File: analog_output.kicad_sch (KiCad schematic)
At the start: 18 parts, among them J3 5 Pin 3.5mm, U6 LM358, U7 74HC14

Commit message: routed version
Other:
- moved on the sheet: U7D
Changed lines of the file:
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@@
   )
   (no_connect (at 172.72 95.25))
-  (no_connect (at 171.45 110.49))
+  (no_connect (at 173.99 110.49))
   (wire (pts (xy 212.09 107.95) (xy 212.09 118.11))
     (stroke (width 0) (type default))
@@
     )
   )
-  (symbol (lib_id "power:GND") (at 156.21 110.49 270) (mirror x) (unit 1)
-    (in_bom yes) (on_board yes) (dnp no) (fields_autoplaced)
-    (property "Reference" "#PWR0143" (at 149.86 110.49 0)
-      (effects (font (size 1.27 1.27)) hide)
-    )
-    (property "Value" "GND" (at 152.4 110.4899 90)
+  (symbol (lib_id "power:GND") (at 158.75 110.49 270) (mirror x) (unit 1)
+    (in_bom yes) (on_board yes) (dnp no) (fields_autoplaced)
+    (property "Reference" "#PWR0143" (at 152.4 110.49 0)
+      (effects (font (size 1.27 1.27)) hide)
+    )
+    (property "Value" "GND" (at 154.94 110.4899 90)
       (effects (font (size 1.27 1.27)) (justify right))
     )
-    (property "Footprint" "" (at 156.21 110.49 0)
-      (effects (font (size 1.27 1.27)) hide)
-    )
-    (property "Datasheet" "" (at 156.21 110.49 0)
+    (property "Footprint" "" (at 158.75 110.49 0)
+      (effects (font (size 1.27 1.27)) hide)
+    )
+    (property "Datasheet" "" (at 158.75 110.49 0)
       (effects (font (size 1.27 1.27)) hide)
     )
@@
     )
   )
-  (symbol (lib_id "74xx:74HC14") (at 163.83 110.49 0) (unit 4)
-    (in_bom yes) (on_board yes) (dnp no) (fields_autoplaced)
-    (property "Reference" "U7" (at 163.83 102.87 0)
-      (effects (font (size 1.27 1.27)))
-    )
-    (property "Value" "74HC14" (at 163.83 105.41 0)
-      (effects (font (size 1.27 1.27)))
-    )
-    (property "Footprint" "Package_SO:SOIC-14_3.9x8.7mm_P1.27mm" (at 163.83 110.49 0)
-      (effects (font (size 1.27 1.27)) hide)
-    )
-    (property "Datasheet" "http://www.ti.com/lit/gpn/sn74HC14" (at 163.83 110.49 0)
-      (effects (font (size 1.27 1.27)) hide)
-    )
-    (property "LCSC" "C5605" (at 163.83 110.49 0)
-      (effects (font (size 1.27 1.27)) hide)
-    )
-    (property "JLCPCB Rotation Offset" "-90" (at 163.83 110.49 0)
+  (symbol (lib_id "74xx:74HC14") (at 166.37 110.49 0) (unit 4)
+    (in_bom yes) (on_board yes) (dnp no) (fields_autoplaced)
+    (property "Reference" "U7" (at 166.37 102.87 0)
+      (effects (font (size 1.27 1.27)))
+    )
+    (property "Value" "74HC14" (at 166.37 105.41 0)
+      (effects (font (size 1.27 1.27)))
+    )
+    (property "Footprint" "Package_SO:SOIC-14_3.9x8.7mm_P1.27mm" (at 166.37 110.49 0)
+      (effects (font (size 1.27 1.27)) hide)
+    )
+    (property "Datasheet" "http://www.ti.com/lit/gpn/sn74HC14" (at 166.37 110.49 0)
+      (effects (font (size 1.27 1.27)) hide)
+    )
+    (property "LCSC" "C5605" (at 166.37 110.49 0)
+      (effects (font (size 1.27 1.27)) hide)
+    )
+    (property "JLCPCB Rotation Offset" "-90" (at 166.37 110.49 0)
       (effects (font (size 1.27 1.27)) hide)
     )
@@
       (effects (font (size 1.27 1.27)) hide)
     )
-    (property "Value" "GND" (at 203.2 130.81 0)
-      (effects (font (size 1.27 1.27)))
-    )
+    (property "Value" "GND" (at 203.2 137.16 0)
+      (effects (font (size 1.27 1.27)))
+    )

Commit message: snap
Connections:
- net GNDA is gone; now on net GND: R14.1, R15.1
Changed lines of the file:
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@@
     )
   )
-  (symbol (lib_id "power:GNDA") (at 76.2 96.52 270) (unit 1)
-    (in_bom yes) (on_board yes) (dnp no) (fields_autoplaced)
-    (property "Reference" "#PWR082" (at 69.85 96.52 0)
-      (effects (font (size 1.27 1.27)) hide)
-    )
-    (property "Value" "GNDA" (at 74.93 93.98 90)
-      (effects (font (size 1.27 1.27)))
+  (symbol (lib_id "power:GND") (at 76.2 96.52 270) (mirror x) (unit 1)
+    (in_bom yes) (on_board yes) (dnp no) (fields_autoplaced)
+    (property "Reference" "#PWR081" (at 69.85 96.52 0)
+      (effects (font (size 1.27 1.27)) hide)
+    )
+    (property "Value" "GND" (at 72.39 96.5199 90)
+      (effects (font (size 1.27 1.27)) (justify right))
     )
     (property "Footprint" "" (at 76.2 96.52 0)
@@
     )
     (property "Datasheet" "" (at 76.2 96.52 0)
-      (effects (font (size 1.27 1.27)) hide)
-    )
-    (pin "1")
-    (instances
-      (project "PiPico_OpenPLC"
-        (path "/6aa34a11-7f01-4bb8-897b-5dd5241ec8f1/2a970fc1-9026-4c1d-bcde-2b8be11d1aad"
-          (reference "#PWR082") (unit 1)
-        )
-      )
-    )
-  )
-  (symbol (lib_id "power:GNDA") (at 74.93 60.96 270) (unit 1)
-    (in_bom yes) (on_board yes) (dnp no) (fields_autoplaced)
-    (property "Reference" "#PWR081" (at 68.58 60.96 0)
-      (effects (font (size 1.27 1.27)) hide)
-    )
-    (property "Value" "GNDA" (at 73.66 58.42 90)
-      (effects (font (size 1.27 1.27)))
-    )
-    (property "Footprint" "" (at 74.93 60.96 0)
-      (effects (font (size 1.27 1.27)) hide)
-    )
-    (property "Datasheet" "" (at 74.93 60.96 0)
       (effects (font (size 1.27 1.27)) hide)
     )
@@
         )
       )
+    )
+  )
+  (symbol (lib_id "power:GND") (at 74.93 60.96 270) (mirror x) (unit 1)
+    (in_bom yes) (on_board yes) (dnp no) (fields_autoplaced)
+    (property "Reference" "#PWR082" (at 68.58 60.96 0)
+      (effects (font (size 1.27 1.27)) hide)
+    )
+    (property "Value" "GND" (at 71.12 60.9599 90)
+      (effects (font (size 1.27 1.27)) (justify right))
+    )
+    (property "Footprint" "" (at 74.93 60.96 0)
+      (effects (font (size 1.27 1.27)) hide)
+    )
+    (property "Datasheet" "" (at 74.93 60.96 0)
+      (effects (font (size 1.27 1.27)) hide)
+    )
+    (pin "1")
+    (instances
+      (project "PiPico_OpenPLC"
+        (path "/6aa34a11-7f01-4bb8-897b-5dd5241ec8f1/2a970fc1-9026-4c1d-bcde-2b8be11d1aad"
+          (reference "#PWR082") (unit 1)
+        )
+      )

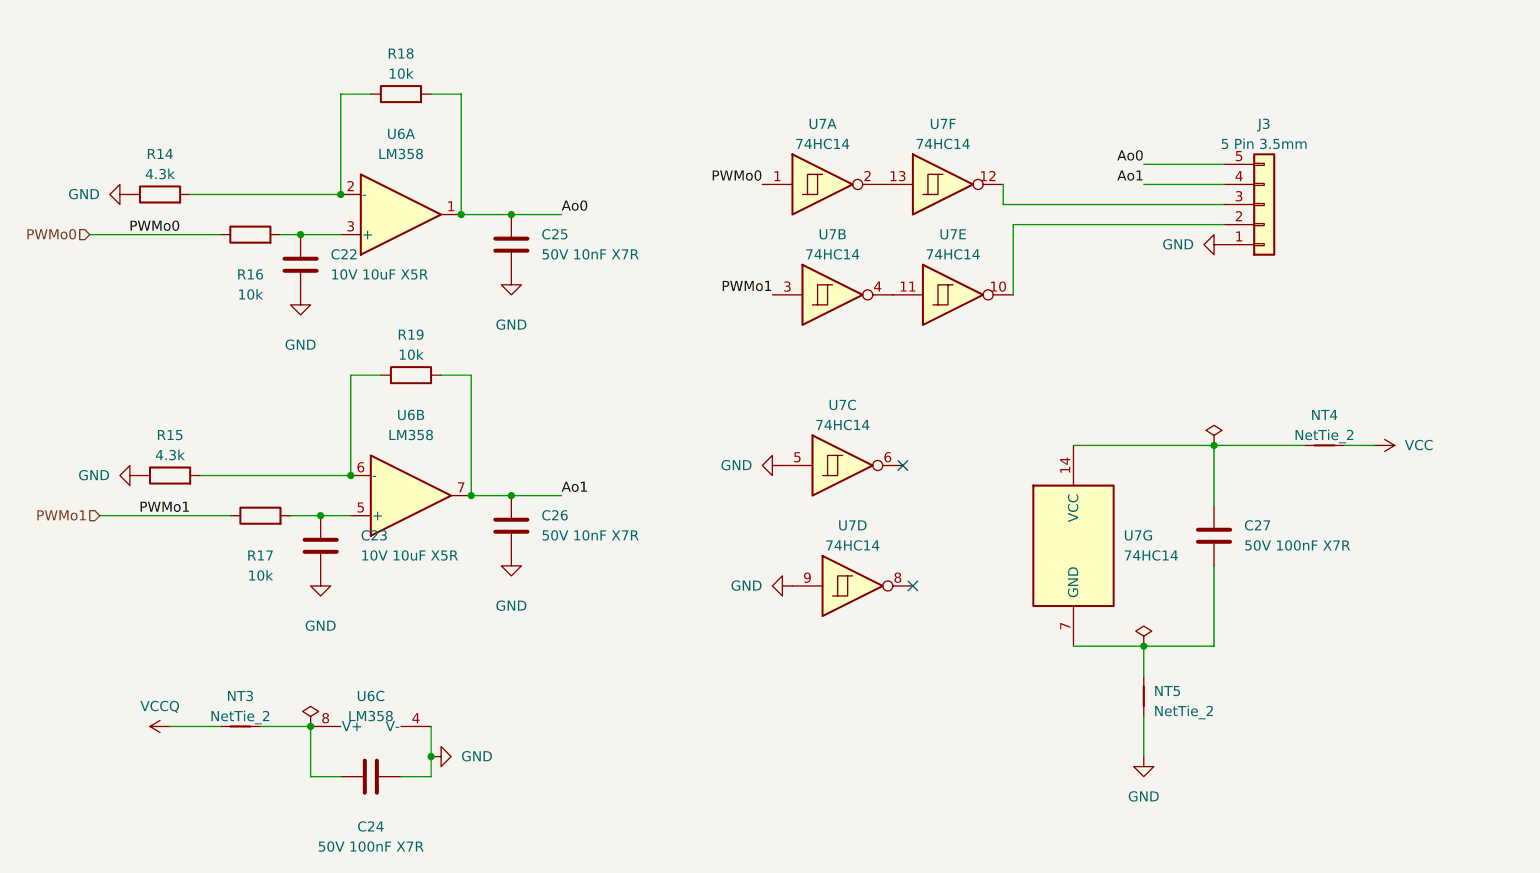
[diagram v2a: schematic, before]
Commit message: Preparation for future use.
Reworked to use i2c bus expanders.
added sketch for add-on boards.
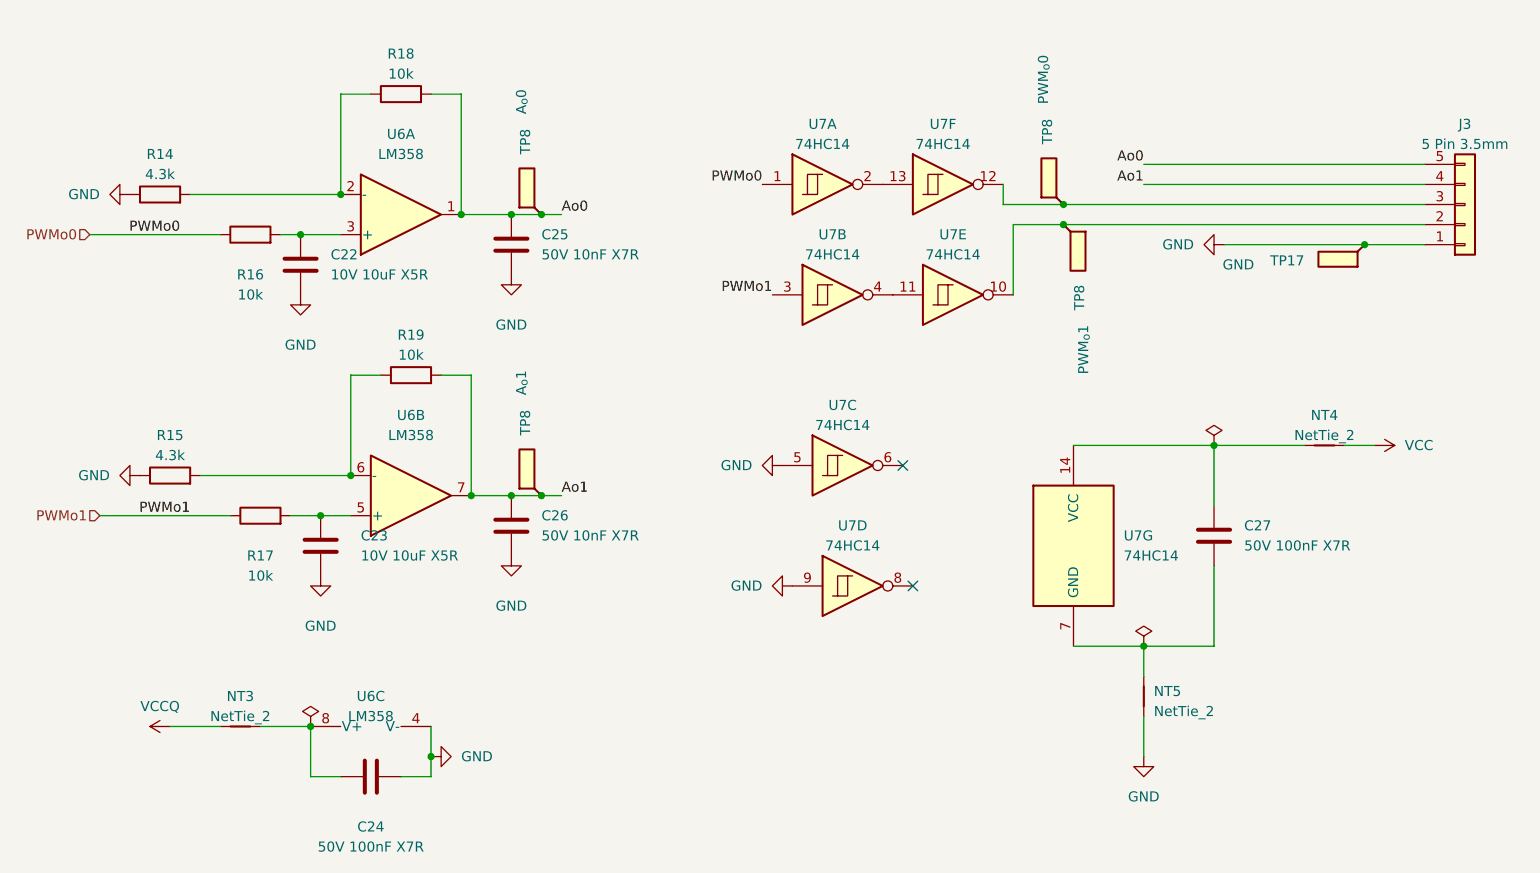
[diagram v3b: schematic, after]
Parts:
- added TP17: GND, TestPoint:TestPoint_Pad_1.0x1.0mm, symbol Connector:TestPoint_Flag
- added TP8: PWM_{o}0, TestPoint:TestPoint_Pad_1.0x1.0mm, symbol Connector:TestPoint_Flag
- added TP8: A_{o}1, TestPoint:TestPoint_Pad_1.0x1.0mm, symbol Connector:TestPoint_Flag
- added TP8: PWM_{o}1, TestPoint:TestPoint_Pad_1.0x1.0mm, symbol Connector:TestPoint_Flag
- added TP8: A_{o}0, TestPoint:TestPoint_Pad_1.0x1.0mm, symbol Connector:TestPoint_Flag
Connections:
- net Ao0: now also TP8.1
- net Ao1: now also TP8.1
- net GND: now also TP17.1
- net at J3.2 (Pin_2), U7.10: now also TP8.1
- net at J3.3 (Pin_3), U7.12: now also TP8.1
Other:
- moved on the sheet: J3
